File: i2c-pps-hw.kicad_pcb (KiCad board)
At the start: 4 copper layers, 85 x 56 mm, 121 parts, among them J1 +5V, J2 Vout, J3 Digital I/O, Q1 SiR880BDP, Q2 SiR880BDP, Q3 SiR880BDP, Q4 SiR880BDP, Q5 SIS413DN, Q6 MMBT3904, Q7 MMBT3904, Q8 SIS413DN, U1 BQ25758S, U2 AP2210-3.3, U3 74AHC1G14

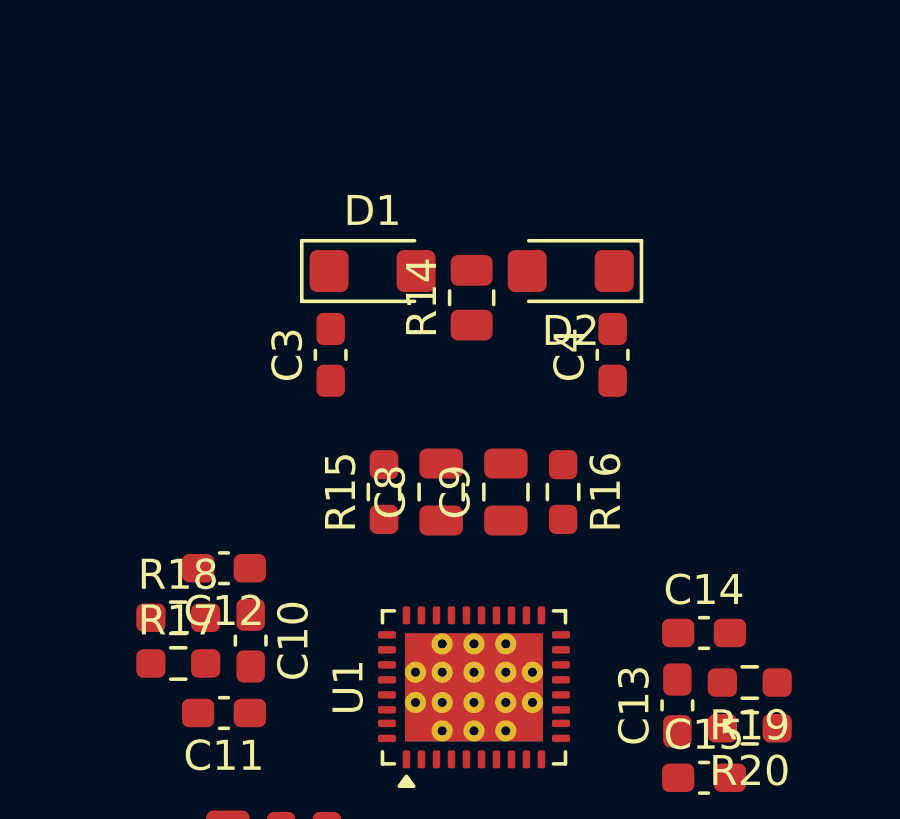
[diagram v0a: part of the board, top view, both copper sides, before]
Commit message: Route driving part of the power stage
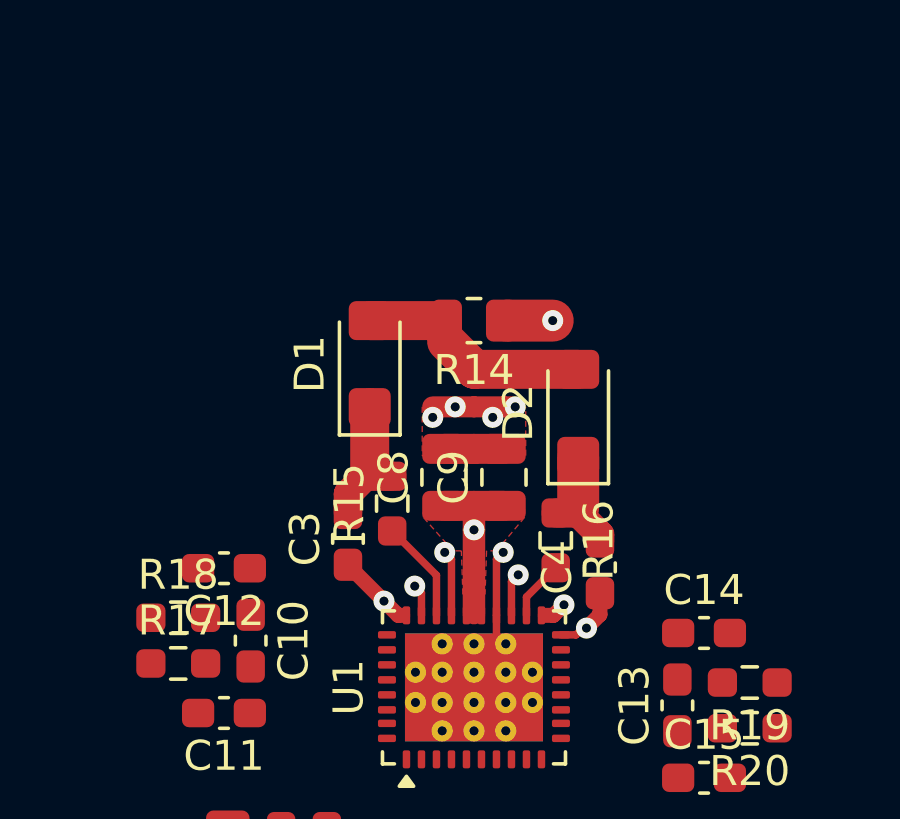
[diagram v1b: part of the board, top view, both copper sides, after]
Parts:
- moved C4 7.10 mm to (142.2, 105.0)
- moved C3 6.16 mm to (133.8, 104.0)
- moved D2 4.73 mm to (141.5, 99.8), turned to 90 degrees
- moved D1 3.10 mm to (134.5, 98.2), turned to 90 degrees
- moved R16 1.63 mm to (140.7, 104.1)
- moved R14 0.77 mm to (138.0, 96.8), turned to 180 degrees
- moved C8 0.50 mm to (137.0, 102.0)
- moved C9 0.49 mm to (139.0, 102.0)
- moved R15 0.47 mm to (135.3, 102.9)
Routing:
- net /Controller and Power Stage/REGN: track 0.00 -> 15.7 mm, vias 0 -> 2
- net Net-(D1-A): track 0.00 -> 7.85 mm
- net GND: track 0.00 -> 7.54 mm, vias 0 -> 5
- net Net-(D1-K): track 0.00 -> 4.53 mm
- net Net-(D2-K): track 0.00 -> 3.64 mm
- net /Controller and Power Stage/BTST1: track 0.00 -> 3.42 mm
- net /Controller and Power Stage/SW1: track 0.00 -> 2.52 mm, vias 0 -> 1
- net /Controller and Power Stage/SW2: track 0.00 -> 2.29 mm, vias 0 -> 1
- net /Controller and Power Stage/LODRV1: track 0.00 -> 2.19 mm, vias 0 -> 1
- net /Controller and Power Stage/BTST2: track 0.00 -> 1.99 mm
- net /Controller and Power Stage/LODRV2: track 0.00 -> 1.44 mm, vias 0 -> 1
- net /Controller and Power Stage/HIDRV1: track 0.00 -> 1.07 mm, vias 0 -> 1
- net /Controller and Power Stage/HIDRV2: track 0.00 -> 0.77 mm, vias 0 -> 1
- added copper zone on F.Cu, net /Controller and Power Stage/REGN
- added copper zone on F.Cu, net GND

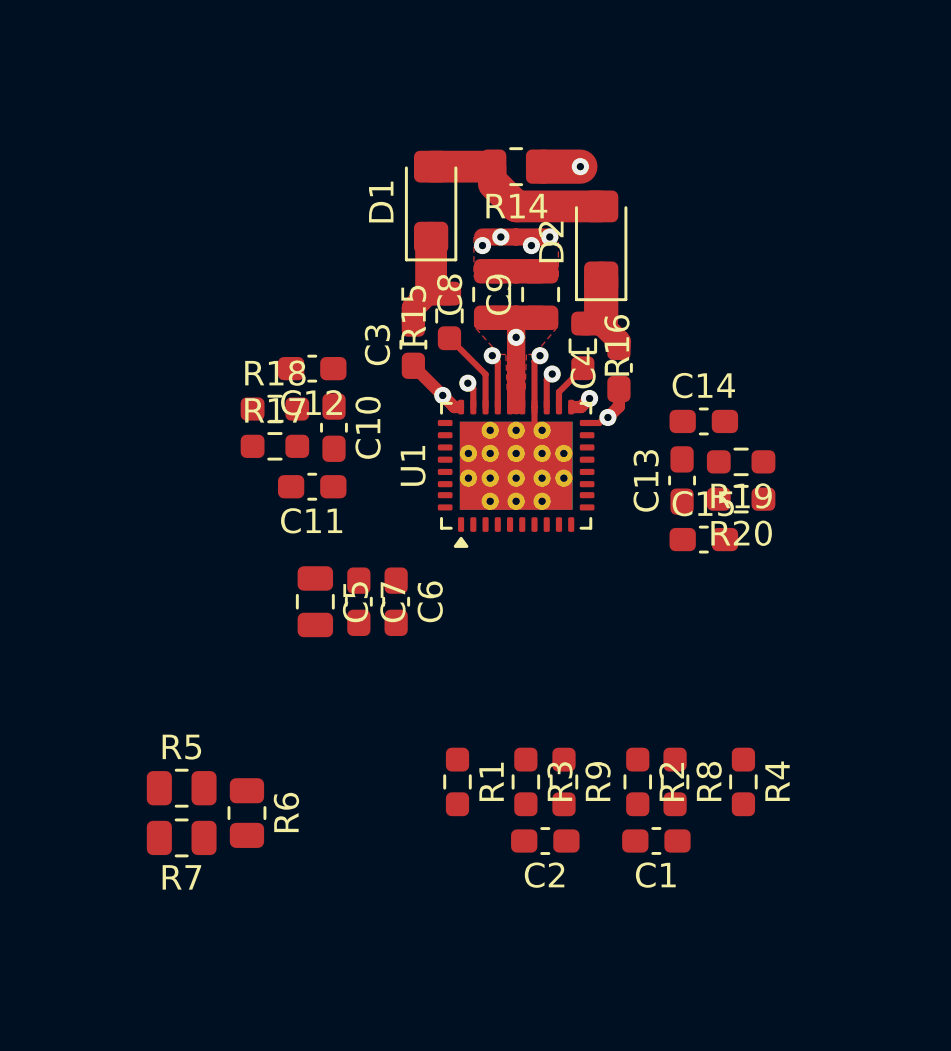
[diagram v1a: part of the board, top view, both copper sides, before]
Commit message: Place and route controller surroundings
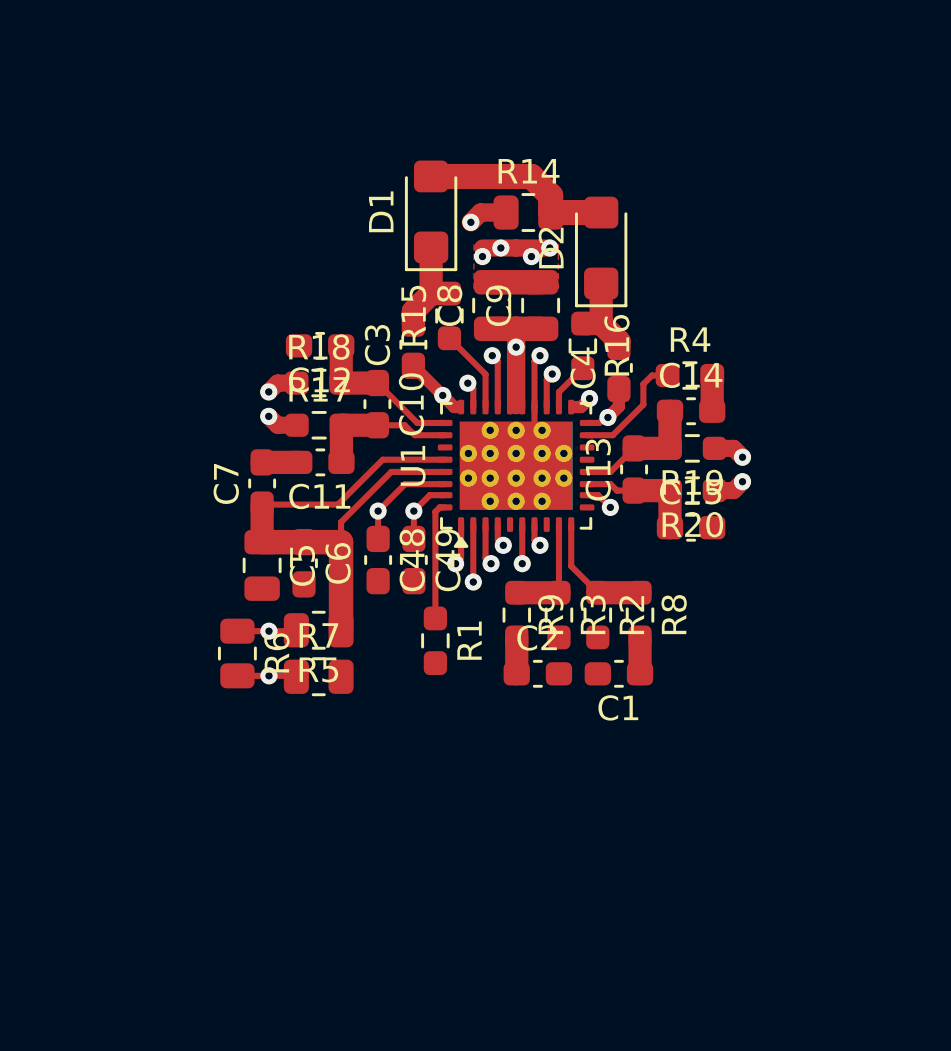
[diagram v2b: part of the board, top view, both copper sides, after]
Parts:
- added C48: 0.1uF, Capacitor_SMD:C_0603_1608Metric_Pad1.08x0.95mm_HandSolder, F.Cu at (132.4, 112.8)
- added C49: 0.1uF, Capacitor_SMD:C_0603_1608Metric_Pad1.08x0.95mm_HandSolder, F.Cu at (133.8, 112.8)
- moved R4 16.8 mm to (145.1, 105.3), turned to 0 degrees
- moved R7 8.64 mm to (129.9, 117.6), turned to 0 degrees
- moved R5 8.54 mm to (129.9, 115.7), turned to 180 degrees
- moved R9 7.09 mm to (138.0, 115.1)
- moved R2 7.01 mm to (141.3, 115.1)
- moved C1 7.00 mm to (142.2, 117.5)
- moved R8 6.97 mm to (143.1, 115.1)
- moved R3 6.95 mm to (139.8, 115.1)
- moved C2 6.84 mm to (138.9, 117.5), turned to 0 degrees
- moved R6 6.53 mm to (126.6, 116.7)
- moved C7 6.24 mm to (127.6, 109.7), turned to 90 degrees
- moved R1 5.84 mm to (134.7, 116.2)
- moved C6 4.08 mm to (129.3, 113.0)
- moved C5 2.63 mm to (127.6, 113.1)
- moved R18 2.09 mm to (129.9, 105.6)
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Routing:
- net /Controller and Power Stage/+5V_Run: track 0.00 -> 23.8 mm, vias 0 -> 1
- net /Controller and Power Stage/ACOV: track 0.00 -> 14.9 mm, vias 0 -> 2
- net /Controller and Power Stage/ACUV: track 0.00 -> 14.3 mm, vias 0 -> 2
- net /Controller and Power Stage/ACN: track 0.00 -> 6.44 mm
- net /Controller and Power Stage/ACP: track 0.00 -> 5.92 mm
- net /Controller and Power Stage/SRN: track 0.00 -> 5.38 mm
- net /Controller and Power Stage/SRP: track 0.00 -> 5.30 mm
- net /Controller and Power Stage/IIN: track 0.00 -> 4.96 mm
- net /Controller and Power Stage/FSW_SYNC: track 0.00 -> 4.83 mm
- net /Controller and Power Stage/MODE: track 0.00 -> 4.79 mm
- net /Controller and Power Stage/IOUT: track 0.00 -> 4.51 mm
- net GND: track 7.54 -> 10.5 mm
- net /Controller and Power Stage/VOUT_Filtered: track 0.00 -> 2.44 mm, vias 0 -> 2
- net /Controller and Power Stage/SDA: track 0.00 -> 2.35 mm, vias 0 -> 1
- net /Controller and Power Stage/REGN: track 15.7 -> 13.5 mm
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- removed copper zone on F.Cu, net /Controller and Power Stage/REGN

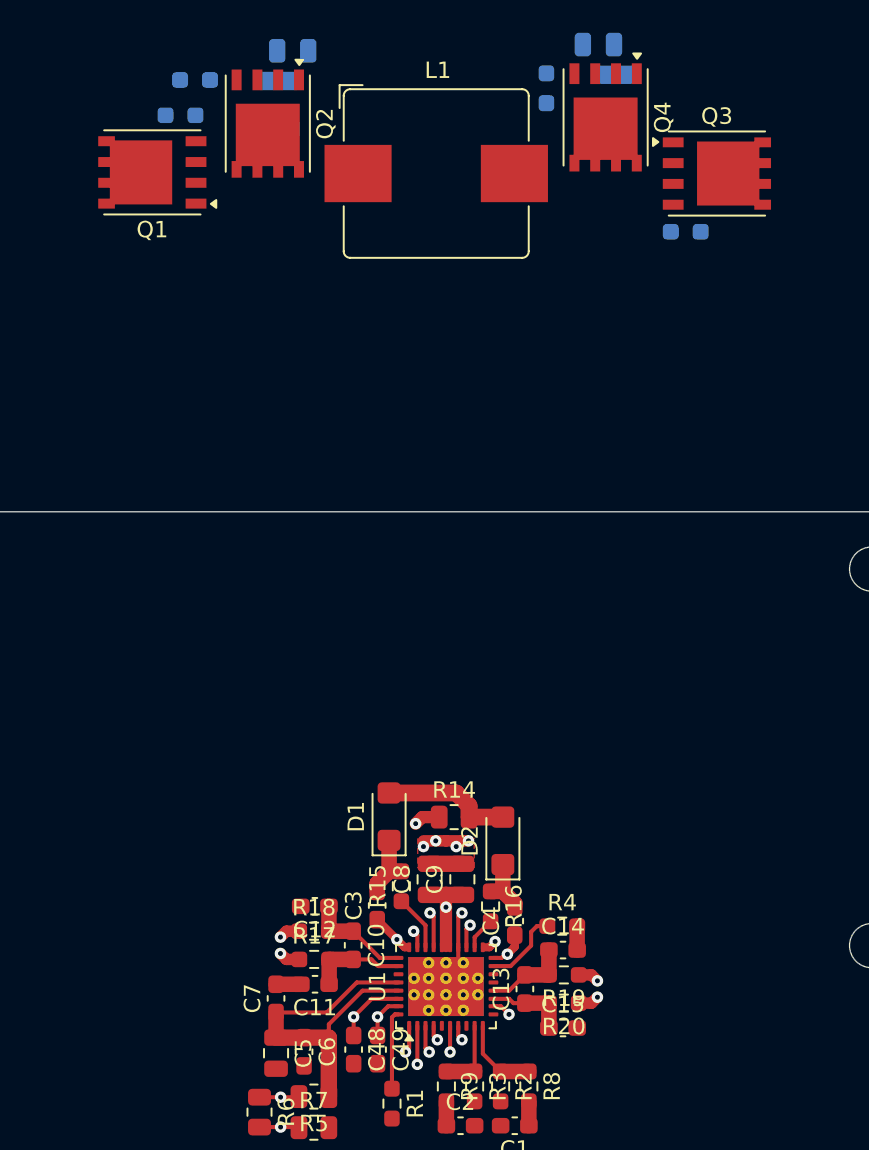
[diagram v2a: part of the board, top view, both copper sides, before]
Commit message: Place and route power stage
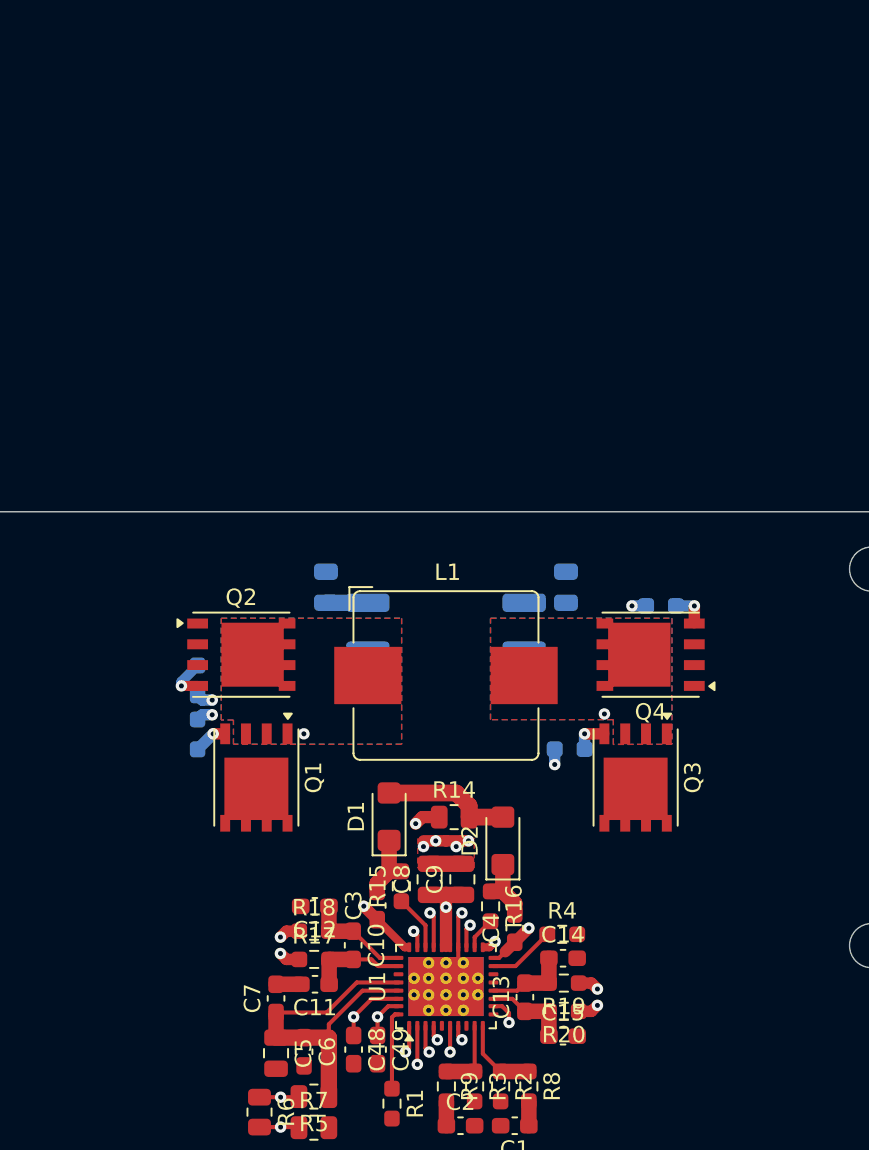
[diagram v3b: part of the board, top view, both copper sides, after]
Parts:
- moved R10 37.8 mm to (122.8, 93.6), turned to -90 degrees
- moved Q1 37.5 mm to (126.4, 96.2), turned to -90 degrees
- moved Q3 37.2 mm to (149.6, 96.2), turned to -90 degrees
- moved R11 36.7 mm to (122.8, 90.3), turned to 90 degrees
- moved C17 33.2 mm to (145.3, 84.6), turned to 90 degrees
- moved Q4 32.9 mm to (150.5, 88.7), turned to 180 degrees
- moved C16 32.8 mm to (130.7, 84.6), turned to 90 degrees
- moved R22 32.7 mm to (142.8, 87.0)
- moved Q2 32.5 mm to (125.5, 88.7), turned to 0 degrees
- moved R12 32.4 mm to (145.6, 94.5)
- moved R13 32.4 mm to (151.1, 85.8), turned to 180 degrees
- moved R21 32.3 mm to (133.2, 87.0)
- moved L1 30.7 mm to (138.0, 90.0)
- moved C13 0.50 mm to (142.8, 109.7)
- moved C14 0.50 mm to (145.2, 107.3)
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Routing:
- net /Controller and Power Stage/LODRV2: track 1.44 -> 27.2 mm, vias 1 -> 2
- net /Controller and Power Stage/LODRV1: track 2.19 -> 25.5 mm, vias 1 -> 2
- net /Controller and Power Stage/HIDRV1: track 1.07 -> 23.8 mm, vias 1 -> 2
- net /Controller and Power Stage/SW2: track 2.29 -> 17.9 mm, vias 1 -> 2
- net /Controller and Power Stage/HIDRV2: track 0.77 -> 14.0 mm, vias 1 -> 2
- net /Controller and Power Stage/SW1: track 2.52 -> 15.7 mm, vias 1 -> 2
- net Net-(Q2-G): track 0.00 -> 2.65 mm, vias 0 -> 1
- net Net-(C16-Pad1): track 0.00 -> 2.56 mm
- net Net-(Q4-G): track 0.00 -> 2.15 mm, vias 0 -> 1
- net Net-(Q3-G): track 0.00 -> 2.10 mm, vias 0 -> 1
- net Net-(Q1-G): track 0.00 -> 2.03 mm, vias 0 -> 1
- net GND: track 10.5 -> 9.06 mm
- net /Controller and Power Stage/MODE: track 4.79 -> 4.09 mm
- net /Controller and Power Stage/VOUT_Filtered: track 2.44 -> 2.99 mm
- added copper zone on B.Cu, net /Controller and Power Stage/SW1
- added copper zone on F.Cu, net /Controller and Power Stage/SW1
- added copper zone on B.Cu, net /Controller and Power Stage/SW2
- added copper zone on F.Cu, net /Controller and Power Stage/SW2

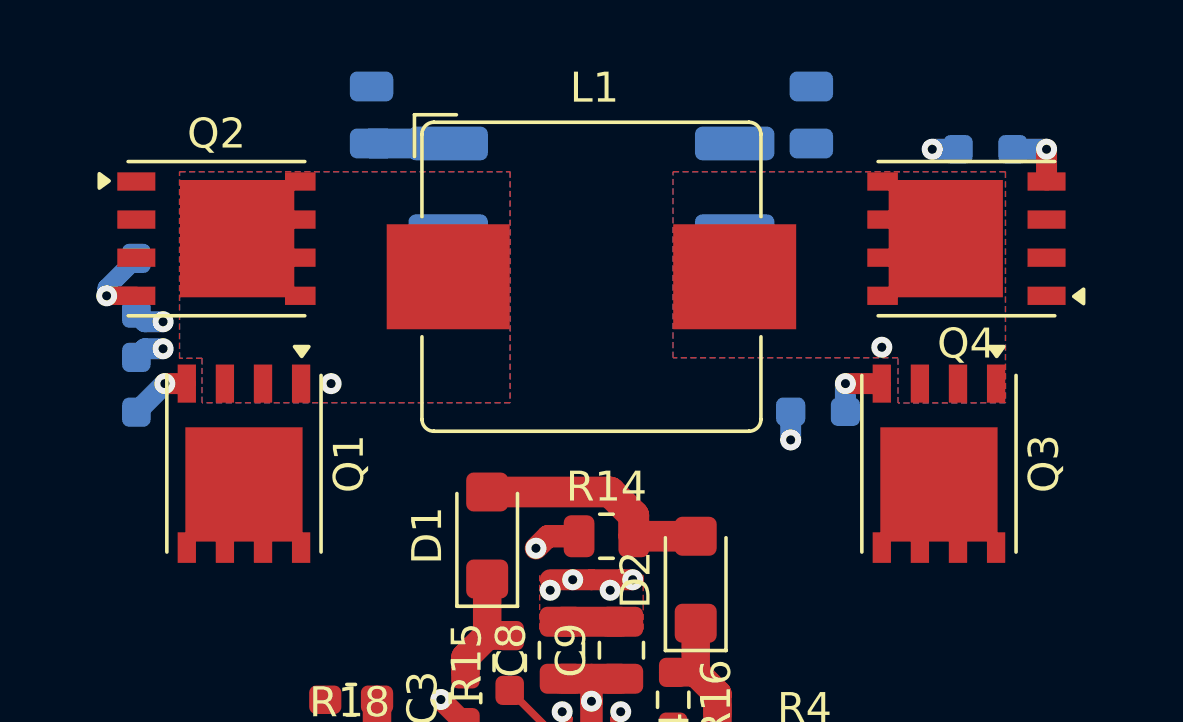
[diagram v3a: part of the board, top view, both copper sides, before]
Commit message: Add thermal vias to the power stage transistors
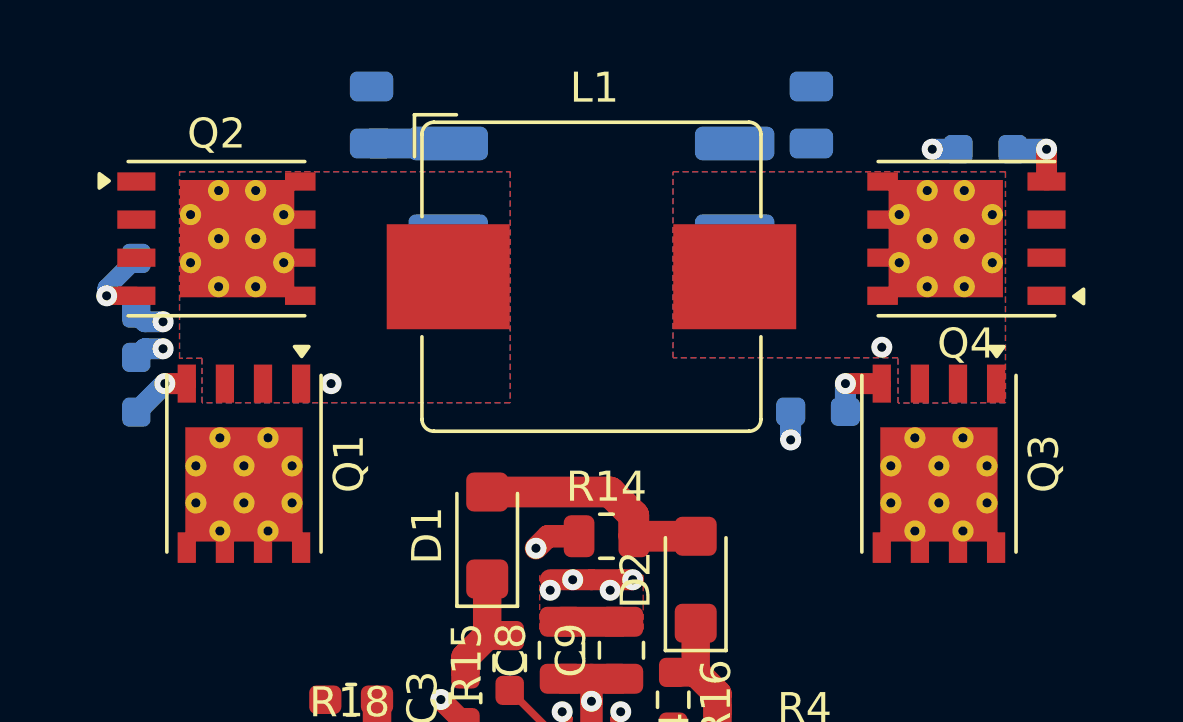
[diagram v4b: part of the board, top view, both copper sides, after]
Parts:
- Q1, Q2, Q3, Q4: footprint Package_SO:PowerPAK_SO-8_Single -> i2c-pps-hw:PowerPAK_SO-8_Single_ThermalVias
